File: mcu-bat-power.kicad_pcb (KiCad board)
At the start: 2 copper layers, 58.6 x 90.9 mm, 59 parts, among them IC1 CN3058E, IC2 HY2112, J1 USB_B_Micro, J2 INDICATORS, J3 PWR, J4 USB, J5 PWR, Q1 FS8205, Q2 2N7002, Q3 2N7002, SW1 SW_SPDT, U1 MT3608, U2 INA219AxD

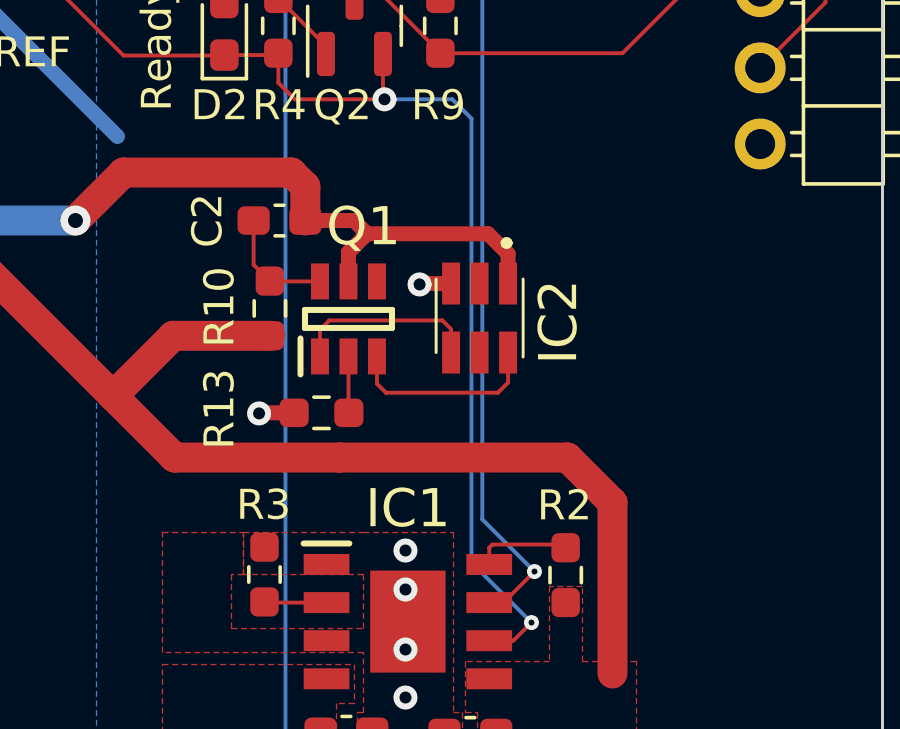
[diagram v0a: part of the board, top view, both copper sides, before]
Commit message: Corrected VDD and VSS connection on HY chip
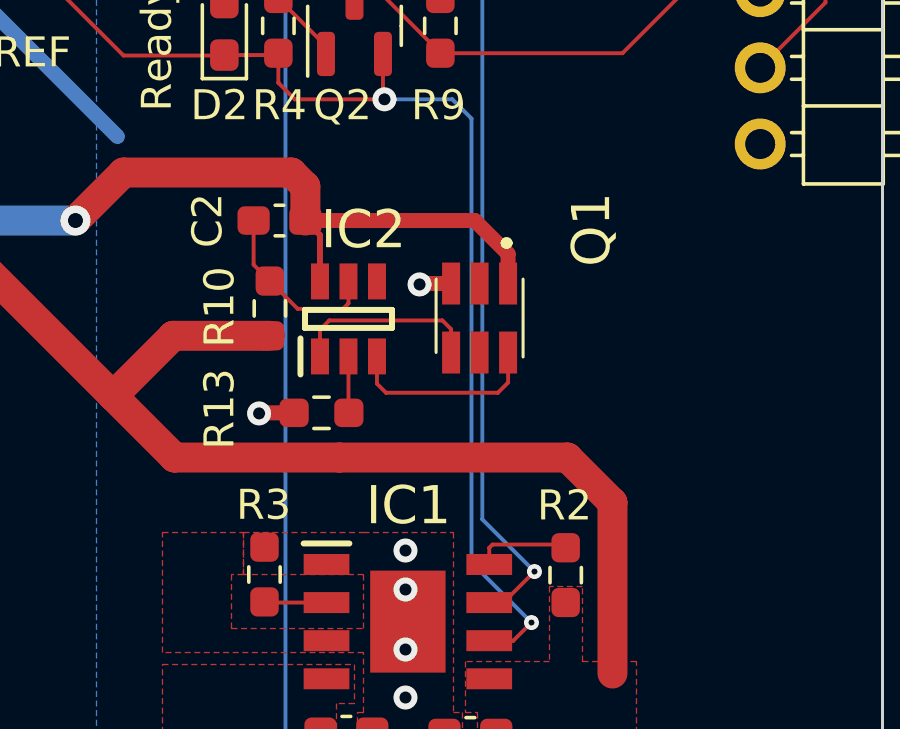
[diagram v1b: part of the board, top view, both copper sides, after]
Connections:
- C2 pad 1: Net-(IC2-VSS) -> Net-(IC2-VDD)
- IC2 pad 5: BAT- -> Net-(IC2-VDD)
- IC2 pad 6: Net-(IC2-VSS) -> BAT-
- R10 pad 1: Net-(IC2-VSS) -> Net-(IC2-VDD)
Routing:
- net Net-(IC2-VDD): track 0.00 -> 6.05 mm
- net Net-(IC2-VSS): track 3.92 -> 0.00 mm
